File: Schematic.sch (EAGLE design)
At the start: 16 parts, among them IC1 7805TV, IC2 ATMEGA168-PU, IC3 LM35CZ, T1 TIP122

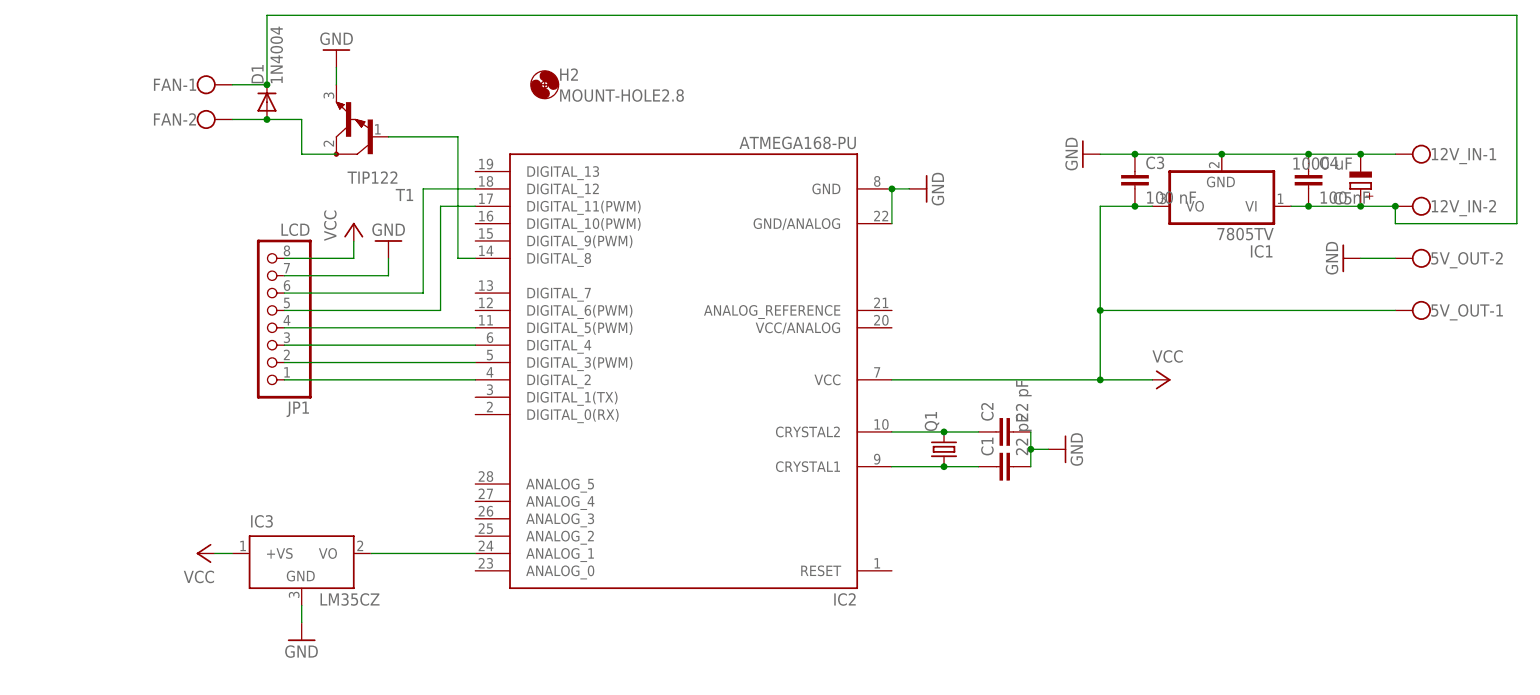
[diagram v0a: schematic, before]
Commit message: Update V1.2
Decoupling capacitor + resistor
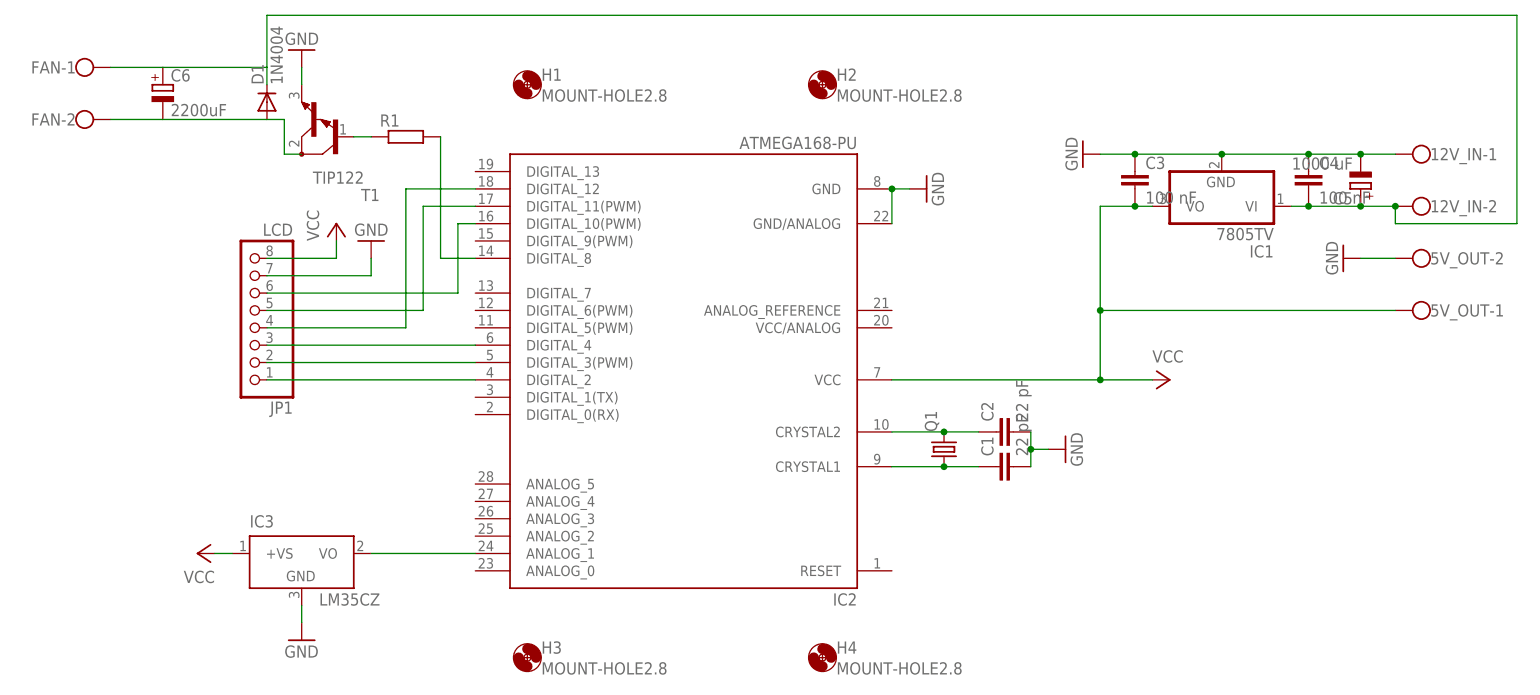
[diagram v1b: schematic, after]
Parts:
- added C6: 2200uF, resistor:CPOL-EUE3.5-10
- added H1, H3, H4: MOUNT-HOLE2.8, holes:MOUNT-HOLE2.8
- added R1: (no value), rcl:R-EU_0207/10
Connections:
- removed net N$13: D1.A, FAN-2.KL, T1.C
- new net N$18: 12V_IN-2.KL, C4.2, C5.+, C6.+, D1.C, FAN-1.KL, IC1.VI
- new net N$2: IC2.DIGITAL_10(PWM), JP1.6
- net N$11: now also JP1.4; no longer JP1.6
- net N$12: now also R1.2; no longer T1.B
- net N$3: now also C6.-, D1.A, FAN-2.KL, T1.C; no longer 12V_IN-2.KL, C4.2, C5.+, D1.C, FAN-1.KL, IC1.VI
- net N$9: now also R1.1, T1.B; no longer IC2.DIGITAL_5(PWM), JP1.4
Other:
- moved on the sheet: FAN-1, FAN-2, H2, JP1, T1
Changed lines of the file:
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@@
 <part name="GND6" library="supply1" deviceset="GND" device=""/>
 <part name="FAN" library="con-wago-500" deviceset="W237-102" device=""/>
-<part name="H2" library="holes" deviceset="MOUNT-HOLE" device="2.8"/>
 <part name="IC3" library="lm35" deviceset="LM35" device="CZ"/>
 <part name="GND7" library="supply1" deviceset="GND" device=""/>
 <part name="P+5" library="supply1" deviceset="VCC" device=""/>
 <part name="P+1" library="supply1" deviceset="VCC" device=""/>
+<part name="H1" library="holes" deviceset="MOUNT-HOLE" device="2.8"/>
+<part name="H2" library="holes" deviceset="MOUNT-HOLE" device="2.8"/>
+<part name="H3" library="holes" deviceset="MOUNT-HOLE" device="2.8"/>
+<part name="H4" library="holes" deviceset="MOUNT-HOLE" device="2.8"/>
+<part name="R1" library="rcl" deviceset="R-EU_" device="0207/10"/>
+<part name="C6" library="resistor" deviceset="CPOL-EU" device="E3.5-10" value="2200uF"/>
 </parts>
 <sheets>
@@
 <instance part="5V_OUT" gate="-1" x="170.18" y="81.28" rot="R180"/>
 <instance part="5V_OUT" gate="-2" x="170.18" y="88.9" rot="R180"/>
-<instance part="T1" gate="G$1" x="15.24" y="106.68" rot="R180"/>
+<instance part="T1" gate="G$1" x="10.16" y="106.68" rot="R180"/>
 <instance part="D1" gate="1" x="0" y="111.76" rot="R90"/>
 <instance part="GND1" gate="1" x="119.38" y="104.14" rot="R270"/>
@@
 <instance part="GND3" gate="1" x="116.84" y="60.96" rot="R90"/>
 <instance part="GND4" gate="1" x="157.48" y="88.9" rot="R270"/>
-<instance part="JP1" gate="A" x="0" y="81.28" rot="R180"/>
-<instance part="GND5" gate="1" x="17.78" y="91.44" rot="R180"/>
-<instance part="P+4" gate="VCC" x="12.7" y="93.98"/>
-<instance part="GND6" gate="1" x="10.16" y="119.38" rot="R180"/>
-<instance part="FAN" gate="-1" x="-10.16" y="114.3"/>
-<instance part="FAN" gate="-2" x="-10.16" y="109.22"/>
-<instance part="H2" gate="G$1" x="40.64" y="114.3"/>
+<instance part="JP1" gate="A" x="-2.54" y="81.28" rot="R180"/>
+<instance part="GND5" gate="1" x="15.24" y="91.44" rot="R180"/>
+<instance part="P+4" gate="VCC" x="10.16" y="93.98"/>
+<instance part="GND6" gate="1" x="5.08" y="119.38" rot="R180"/>
+<instance part="FAN" gate="-1" x="-27.94" y="116.84"/>
+<instance part="FAN" gate="-2" x="-27.94" y="109.22"/>
 <instance part="IC3" gate="G$1" x="5.08" y="45.72"/>
 <instance part="GND7" gate="1" x="5.08" y="33.02"/>
 <instance part="P+5" gate="VCC" x="-10.16" y="45.72" rot="R90"/>
 <instance part="P+1" gate="VCC" x="132.08" y="71.12" rot="R270"/>
+<instance part="H1" gate="G$1" x="38.1" y="114.3"/>
+<instance part="H2" gate="G$1" x="81.28" y="114.3"/>
+<instance part="H3" gate="G$1" x="38.1" y="30.48"/>
+<instance part="H4" gate="G$1" x="81.28" y="30.48"/>
+<instance part="R1" gate="G$1" x="20.32" y="106.68"/>
+<instance part="C6" gate="G$1" x="-15.24" y="114.3"/>
 </instances>
 <busses>
 </busses>
 <nets>
-<net name="N$3" class="0">
+<net name="N$18" class="0">
 <segment>
 <pinref part="D1" gate="1" pin="C"/>
-<wire x1="0" y1="114.3" x2="0" y2="124.46" width="0.1524" layer="91"/>
+<wire x1="0" y1="114.3" x2="0" y2="116.84" width="0.1524" layer="91"/>
+<wire x1="0" y1="116.84" x2="0" y2="124.46" width="0.1524" layer="91"/>
 <wire x1="0" y1="124.46" x2="182.88" y2="124.46" width="0.1524" layer="91"/>
-<pinref part="FAN" gate="-1" pin="KL"/>
-<wire x1="-5.08" y1="114.3" x2="0" y2="114.3" width="0.1524" layer="91"/>
-<junction x="0" y="114.3"/>
 <wire x1="182.88" y1="124.46" x2="182.88" y2="93.98" width="0.1524" layer="91"/>
 <pinref part="C4" gate="G$1" pin="2"/>
@@
 <wire x1="165.1" y1="93.98" x2="165.1" y2="96.52" width="0.1524" layer="91"/>
 <junction x="165.1" y="96.52"/>
+<pinref part="FAN" gate="-1" pin="KL"/>
+<pinref part="C6" gate="G$1" pin="+"/>
+<wire x1="-22.86" y1="116.84" x2="-15.24" y2="116.84" width="0.1524" layer="91"/>
+<wire x1="-15.24" y1="116.84" x2="0" y2="116.84" width="0.1524" layer="91"/>
 </segment>
 </net>
@@
 <pinref part="JP1" gate="A" pin="7"/>
 <pinref part="GND5" gate="1" pin="GND"/>
-<wire x1="2.54" y1="86.36" x2="17.78" y2="86.36" width="0.1524" layer="91"/>
-<wire x1="17.78" y1="86.36" x2="17.78" y2="88.9" width="0.1524" layer="91"/>
+<wire x1="0" y1="86.36" x2="15.24" y2="86.36" width="0.1524" layer="91"/>
+<wire x1="15.24" y1="86.36" x2="15.24" y2="88.9" width="0.1524" layer="91"/>
 </segment>
 <segment>
 <pinref part="GND6" gate="1" pin="GND"/>
 <pinref part="T1" gate="G$1" pin="E"/>
-<wire x1="10.16" y1="116.84" x2="10.16" y2="114.3" width="0.1524" layer="91"/>
+<wire x1="5.08" y1="116.84" x2="5.08" y2="114.3" width="0.1524" layer="91"/>
 </segment>
 <segment>
@@
 <pinref part="P+4" gate="VCC" pin="VCC"/>
 <pinref part="JP1" gate="A" pin="8"/>
-<wire x1="12.7" y1="91.44" x2="12.7" y2="88.9" width="0.1524" layer="91"/>
-<wire x1="12.7" y1="88.9" x2="2.54" y2="88.9" width="0.1524" layer="91"/>
+<wire x1="10.16" y1="91.44" x2="10.16" y2="88.9" width="0.1524" layer="91"/>
+<wire x1="10.16" y1="88.9" x2="0" y2="88.9" width="0.1524" layer="91"/>
 </segment>
 <segment>
@@
 <net name="N$10" class="0">
 <segment>
-<wire x1="25.4" y1="81.28" x2="25.4" y2="96.52" width="0.1524" layer="91"/>
+<pinref part="IC2" gate="1" pin="DIGITAL_11(PWM)"/>
+<wire x1="22.86" y1="81.28" x2="22.86" y2="96.52" width="0.1524" layer="91"/>
+<wire x1="30.48" y1="96.52" x2="22.86" y2="96.52" width="0.1524" layer="91"/>
 <pinref part="JP1" gate="A" pin="5"/>
-<wire x1="25.4" y1="81.28" x2="2.54" y2="81.28" width="0.1524" layer="91"/>
-<pinref part="IC2" gate="1" pin="DIGITAL_11(PWM)"/>
-<wire x1="30.48" y1="96.52" x2="25.4" y2="96.52" width="0.1524" layer="91"/>
+<wire x1="22.86" y1="81.28" x2="0" y2="81.28" width="0.1524" layer="91"/>
 </segment>
 </net>
@@
 <segment>
 <pinref part="IC2" gate="1" pin="DIGITAL_12"/>
-<wire x1="30.48" y1="99.06" x2="22.86" y2="99.06" width="0.1524" layer="91"/>
-<wire x1="22.86" y1="99.06" x2="22.86" y2="83.82" width="0.1524" layer="91"/>
-<pinref part="JP1" gate="A" pin="6"/>
-<wire x1="22.86" y1="83.82" x2="2.54" y2="83.82" width="0.1524" layer="91"/>
+<wire x1="30.48" y1="99.06" x2="20.32" y2="99.06" width="0.1524" layer="91"/>
+<wire x1="20.32" y1="99.06" x2="20.32" y2="78.74" width="0.1524" layer="91"/>
+<pinref part="JP1" gate="A" pin="4"/>
+<wire x1="0" y1="78.74" x2="20.32" y2="78.74" width="0.1524" layer="91"/>
 </segment>
 </net>
@@
 <pinref part="IC2" gate="1" pin="DIGITAL_3(PWM)"/>
 <pinref part="JP1" gate="A" pin="2"/>
-<wire x1="30.48" y1="73.66" x2="2.54" y2="73.66" width="0.1524" layer="91"/>
+<wire x1="30.48" y1="73.66" x2="0" y2="73.66" width="0.1524" layer="91"/>
 </segment>
 </net>
@@
 <pinref part="IC2" gate="1" pin="DIGITAL_4"/>
 <pinref part="JP1" gate="A" pin="3"/>
-<wire x1="30.48" y1="76.2" x2="2.54" y2="76.2" width="0.1524" layer="91"/>
+<wire x1="30.48" y1="76.2" x2="0" y2="76.2" width="0.1524" layer="91"/>
 </segment>
 </net>
@@
 <segment>
 <pinref part="IC2" gate="1" pin="DIGITAL_8"/>
-<wire x1="30.48" y1="88.9" x2="27.94" y2="88.9" width="0.1524" layer="91"/>
-<wire x1="27.94" y1="88.9" x2="27.94" y2="106.68" width="0.1524" layer="91"/>
-<pinref part="T1" gate="G$1" pin="B"/>
-<wire x1="27.94" y1="106.68" x2="17.78" y2="106.68" width="0.1524" layer="91"/>
-</segment>
-</net>
-<net name="N$13" class="0">
+<wire x1="30.48" y1="88.9" x2="25.4" y2="88.9" width="0.1524" layer="91"/>
+<wire x1="25.4" y1="88.9" x2="25.4" y2="106.68" width="0.1524" layer="91"/>
+<pinref part="R1" gate="G$1" pin="2"/>
+</segment>
+</net>
+<net name="N$3" class="0">
 <segment>
 <pinref part="T1" gate="G$1" pin="C"/>
-<wire x1="10.16" y1="104.14" x2="5.08" y2="104.14" width="0.1524" layer="91"/>
-<wire x1="5.08" y1="104.14" x2="5.08" y2="109.22" width="0.1524" layer="91"/>
+<wire x1="5.08" y1="104.14" x2="2.54" y2="104.14" width="0.1524" layer="91"/>
+<wire x1="2.54" y1="104.14" x2="2.54" y2="109.22" width="0.1524" layer="91"/>
 <pinref part="D1" gate="1" pin="A"/>
-<wire x1="5.08" y1="109.22" x2="0" y2="109.22" width="0.1524" layer="91"/>
+<wire x1="2.54" y1="109.22" x2="0" y2="109.22" width="0.1524" layer="91"/>
 <pinref part="FAN" gate="-2" pin="KL"/>
-<wire x1="-5.08" y1="109.22" x2="0" y2="109.22" width="0.1524" layer="91"/>
-<junction x="0" y="109.22"/>
-</segment>
-</net>
-<net name="N$9" class="0">
-<segment>
-<pinref part="IC2" gate="1" pin="DIGITAL_5(PWM)"/>
-<pinref part="JP1" gate="A" pin="4"/>
-<wire x1="30.48" y1="78.74" x2="2.54" y2="78.74" width="0.1524" layer="91"/>
+<pinref part="C6" gate="G$1" pin="-"/>
+<wire x1="-22.86" y1="109.22" x2="-15.24" y2="109.22" width="0.1524" layer="91"/>
+<wire x1="-15.24" y1="109.22" x2="0" y2="109.22" width="0.1524" layer="91"/>
 </segment>
 </net>
@@
 <pinref part="IC2" gate="1" pin="DIGITAL_2"/>
 <pinref part="JP1" gate="A" pin="1"/>
-<wire x1="30.48" y1="71.12" x2="2.54" y2="71.12" width="0.1524" layer="91"/>
+<wire x1="30.48" y1="71.12" x2="0" y2="71.12" width="0.1524" layer="91"/>
 </segment>
 </net>
@@
 </segment>
 </net>
+<net name="N$2" class="0">
+<segment>
+<pinref part="IC2" gate="1" pin="DIGITAL_10(PWM)"/>
+<wire x1="30.48" y1="93.98" x2="27.94" y2="93.98" width="0.1524" layer="91"/>
+<wire x1="27.94" y1="93.98" x2="27.94" y2="83.82" width="0.1524" layer="91"/>
+<pinref part="JP1" gate="A" pin="6"/>
+<wire x1="0" y1="83.82" x2="27.94" y2="83.82" width="0.1524" layer="91"/>
+</segment>
+</net>
+<net name="N$9" class="0">
+<segment>
+<pinref part="T1" gate="G$1" pin="B"/>
+<pinref part="R1" gate="G$1" pin="1"/>
+<wire x1="12.7" y1="106.68" x2="15.24" y2="106.68" width="0.1524" layer="91"/>
+</segment>
+</net>
